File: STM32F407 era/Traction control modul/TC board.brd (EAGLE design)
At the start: 115.5 x 100 mm, 19 parts, among them IC1 74HC14D, IC2 lm2575, U1 MAX13052ESA+

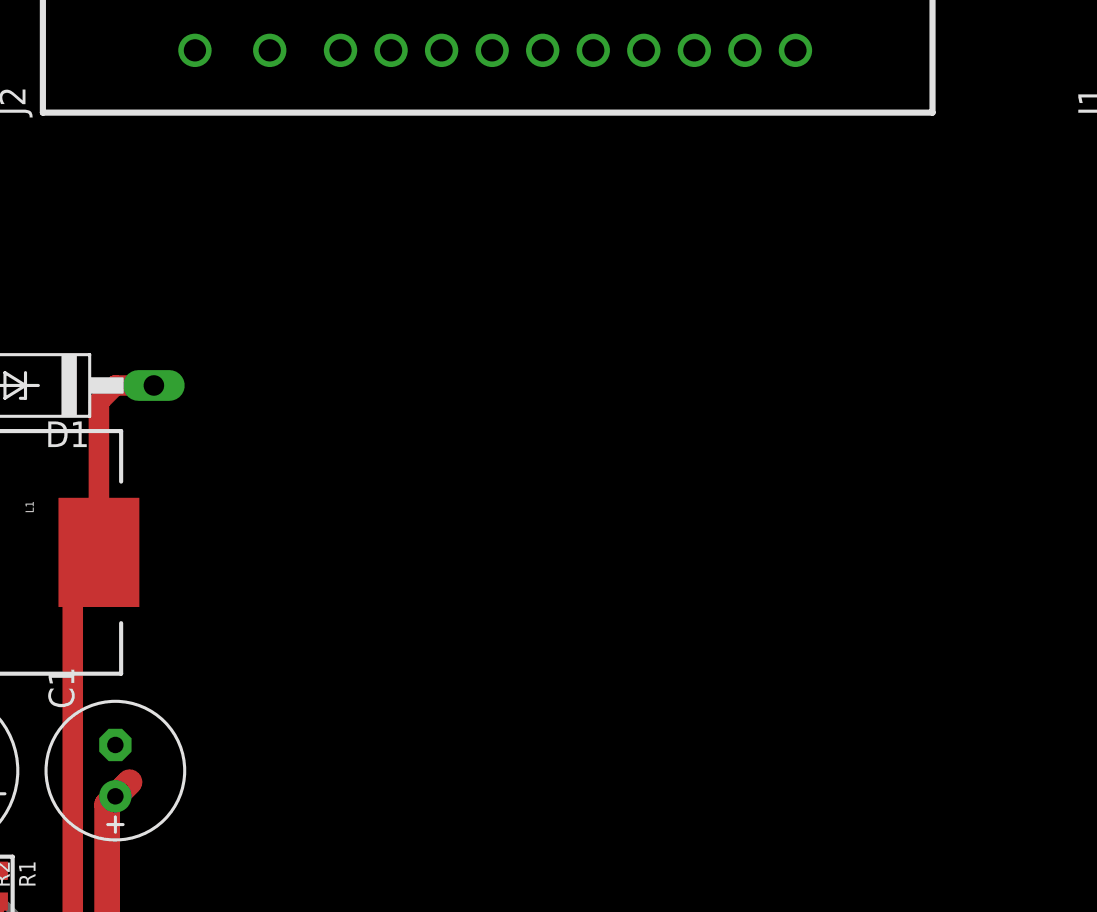
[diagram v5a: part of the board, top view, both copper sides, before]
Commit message: started working on control signals to gear
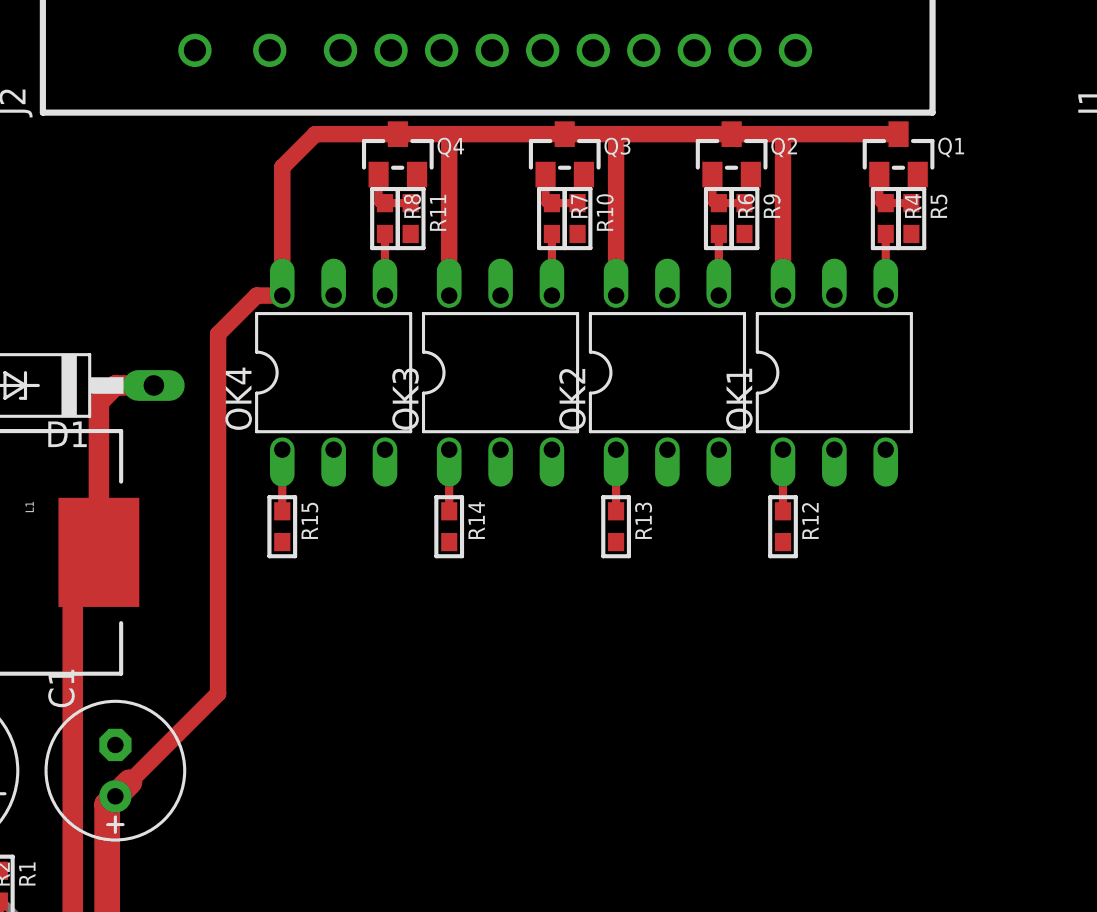
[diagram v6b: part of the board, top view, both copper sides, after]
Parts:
- added OK1, OK2, OK3, OK4: H11L1M, optocoupler:DIL06
- added Q1, Q2, Q3, Q4: (no value), microbuilder:SOT23-WIDE
- added R10, R11, R5, R9: 1000, microbuilder:_0603
- added R12, R13, R14, R15, R4, R6, R7, R8: 200, microbuilder:_0603
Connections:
- new net N$10: Q2.1, R6.1, R9.1
- new net N$11: OK3.4, R7.2
- new net N$12: Q3.1, R10.1, R7.1
- new net N$13: OK4.4, R8.2
- new net N$14: Q4.1, R11.1, R8.1
- new net N$15: OK4.1, R15.1
- new net N$16: OK3.1, R14.1
- new net N$17: OK2.1, R13.1
- new net N$18: OK1.1, R12.1
- new net N$19: R12.2
- new net N$20: R13.2
- new net N$21: R14.2
- new net N$22: R15.2
- new net N$7: OK1.4, R4.2
- new net N$8: Q1.1, R4.1, R5.1
- new net N$9: OK2.4, R6.2
- net 12V: now also OK1.6, OK2.6, OK3.6, OK4.6, Q1.3, Q2.3, Q3.3, Q4.3
- net GND: now also OK1.2, OK1.5, OK2.2, OK2.5, OK3.2, OK3.5, OK4.2, OK4.5, Q1.2, Q2.2, Q3.2, Q4.2, R10.2, R11.2, R5.2, R9.2
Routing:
- net 12V: track 11.6 -> 101.0 mm
- net N$9: track 0.00 -> 3.05 mm
- net N$7: track 0.00 -> 3.05 mm
- net N$18: track 0.00 -> 3.05 mm
- net N$17: track 0.00 -> 3.05 mm
- net N$16: track 0.00 -> 3.05 mm
- net N$15: track 0.00 -> 3.05 mm
- net N$13: track 0.00 -> 3.05 mm
- net N$11: track 0.00 -> 3.05 mm
- net N$8: track 0.00 -> 3.00 mm
- net N$10: track 0.00 -> 3.00 mm
- net N$12: track 0.00 -> 3.00 mm
- net N$14: track 0.00 -> 3.00 mm

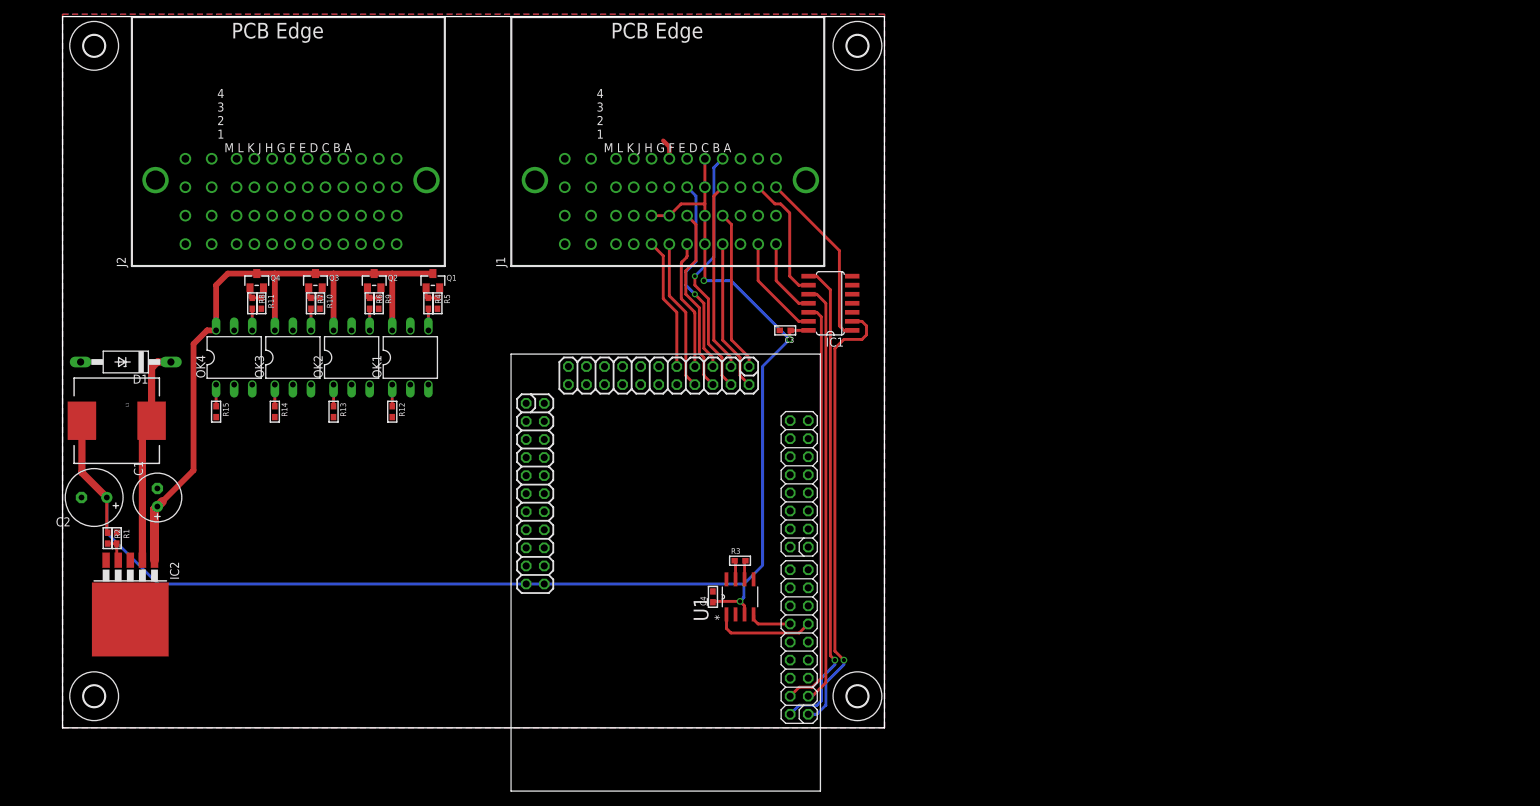
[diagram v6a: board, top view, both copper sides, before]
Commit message: succeded in removing one of 2 connectors
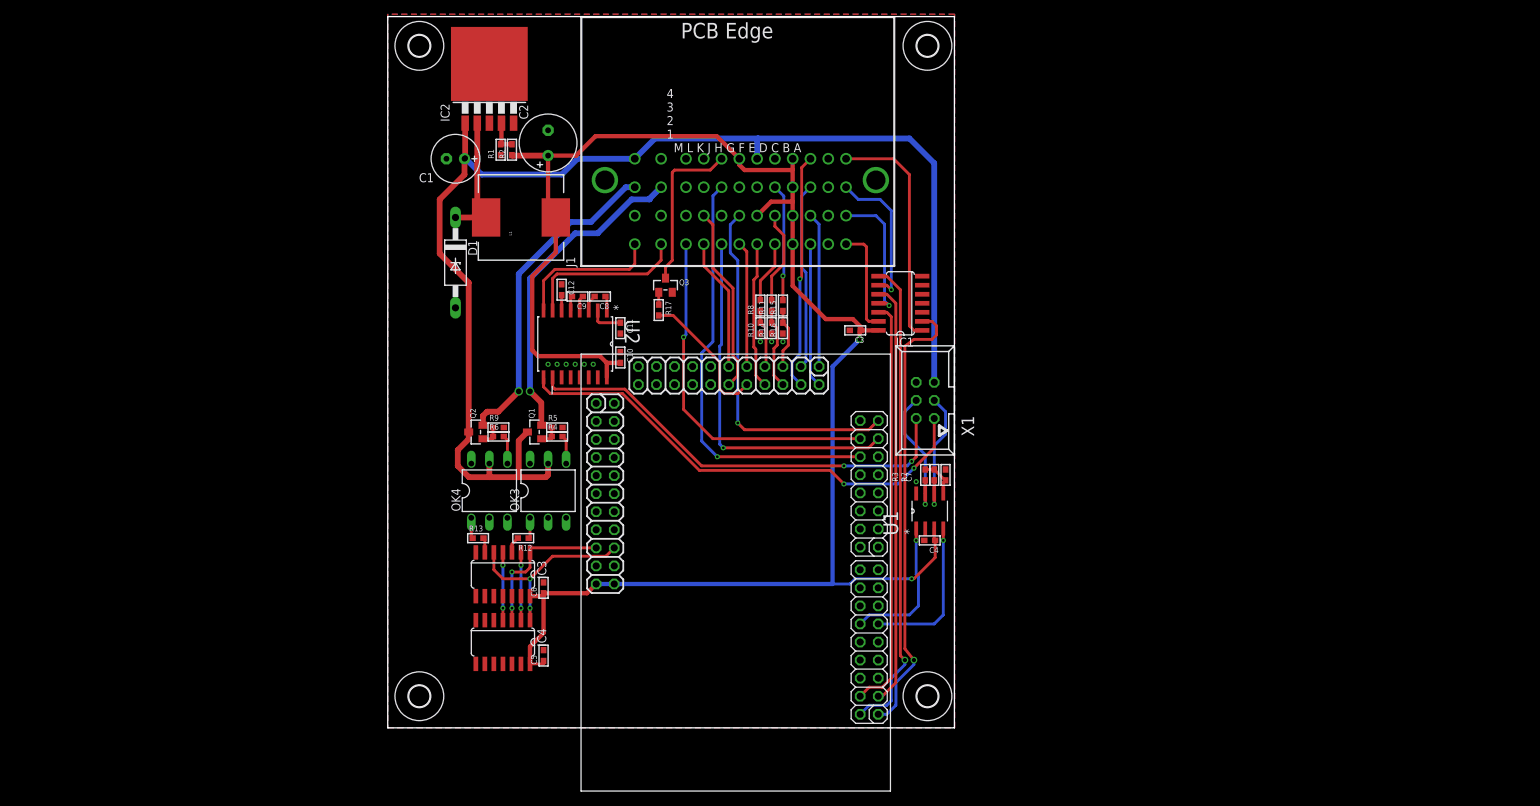
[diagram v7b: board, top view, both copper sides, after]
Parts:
- removed J2: (no value), unicorn_v2:AUTOCONNECTOR
- removed OK1, OK2: H11L1M, optocoupler:DIL06
- removed Q4: (no value), microbuilder:SOT23-WIDE
- added C10, C11, C12, C5, C6, C8, C9: 100n, microbuilder:_0603
- added C7: 4n7, microbuilder:_0603
- added IC3: 74AC08D, 74xx-eu:SO14
- added IC4: 74AC04D, 74xx-eu:SO14
- added R16: 178, microbuilder:_0603
- added R17: 500, microbuilder:_0603
- added U2: MAX232AEWE+, Maxim_By_element14_Batch_1:SOIC127P1032X265-16N
- added X1: 057-006-1, con-panduit:057-006-1
- J1: value (none) -> CON1
- OK3, OK4: value H11L1M -> 4N37
- R10: value 1000 -> 178
- R11: value 1000 -> 604
- R14: value 200 -> 178
- R15, R8: value 200 -> 604
- R3: value 1k8 -> 60
- R7: value 200 -> 60
- moved R7 90.9 mm to (76.8, 35.6), turned to 90 degrees
- moved IC2 88.8 mm to (14.3, 90.8), turned to 0 degrees
- moved R15 81.1 mm to (55.6, 59.4), turned to 90 degrees
- moved C2 81.0 mm to (22.5, 82.2), turned to 90 degrees
- moved R2 78.8 mm to (17.5, 81.3), turned to 90 degrees
- moved R1 76.8 mm to (15.9, 81.3), turned to 90 degrees
- moved R11 71.8 mm to (54.0, 59.4), turned to 90 degrees
- moved R8 71.4 mm to (52.4, 59.4), turned to 90 degrees
- moved R14 70.8 mm to (54.0, 56.2), turned to 90 degrees
- moved L1 63.6 mm to (18.7, 71.8), turned to 90 degrees
- moved C1 63.4 mm to (9.53, 80.0), turned to 180 degrees
- moved R10 62.0 mm to (52.4, 56.2), turned to 90 degrees
- moved Q3 49.2 mm to (39.1, 62.2)
- moved D1 48.4 mm to (9.53, 65.4), turned to 270 degrees
- moved H2 45.7 mm to (4.45, 95.9)
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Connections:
- new net BITEO: R15.1, R16.2, U$1.P$5
- new net BRAKEP: J1.K1, U$1.P$76
- new net COMRX: U2.9, X1.1
- new net COMTX: U2.10, X1.2
- new net DIRA: IC3.1, IC4.3, U$1.P$39
- new net DIRAO: J1.L3, Q1.2
- new net DIRB: IC3.5, IC4.1, U$1.P$40
- new net DIRBO: J1.M3, Q2.2
- new net FUEL1: J1.J3
- new net FUEL2: J1.K3
- new net FUEL3: J1.J4
- new net FUEL4: J1.K4
- new net GSENSO: R10.2, R8.1, U$1.P$7
- new net IGNCUT: R17.2, U$1.P$10
- new net IGNCUTO: J1.H4, Q3.3
- new net N$23: C11.1, U2.2
- new net N$24: Q3.1, R17.1
- new net NEUTRAL: J1.J1, U$1.P$11
- new net OILP: J1.J2, U$1.P$12
- new net RS232RX: J1.M1, U2.8
- new net RS232TX: J1.L1, U2.7
- new net SPEED: J1.G2, U$1.P$77
- new net VTEMP: J1.H1, U$1.P$75
- new net VTEMP2: J1.H3, U$1.P$74
- new net YAWO: R11.1, R14.2, U$1.P$6
- net 12V: now also J1.F4, J1.M4, OK3.5, OK4.5, X1.5; no longer J1.G4, J1.M1, OK1.6, OK2.6, OK3.6, OK4.6, Q3.3, Q4.3
- net 3.3V: now also C10.2, C5.1, C6.1, IC3.14, IC4.14, J1.D1, J1.D2, J1.D3, J1.D4, J1.F2, J1.G4, U2.16; no longer J1.E1, J1.E2, J1.E3, J1.E4, J1.G2, J1.H2
- net BITE: now also J1.E3, R15.2; no longer J1.F3, U$1.P$5
- net BRAKE-POT: now also J1.F1; no longer J1.G1
- net CANH: now also R7.1, X1.3; no longer R3.2
- net CANL: now also X1.4
- net CAN_RX: now also U1.4; no longer U1.1
- net CAN_TX: now also U1.1; no longer U1.4
- net CLUTCH-POT: now also J1.G1; no longer J1.H1
- net GND: now also C10.1, C11.2, C12.1, C5.2, C6.2, C7.2, IC3.10, IC3.12, IC3.13, IC3.7, IC3.9, IC4.11, IC4.13, IC4.5, IC4.7, IC4.9, J1.B1, J1.B3, J1.E4, J1.F3, J1.H2, J1.L4, R10.1, R14.1, R16.1, U2.15, X1.6; no longer J1.A2, J1.A4, J1.C1, J1.C2, J1.C3, J1.C4, J1.F4, J1.H3, J1.L1, OK1.2, OK1.5, OK2.2, OK2.5, OK3.5, OK4.5, Q1.2, Q2.2, Q4.2, R10.2, R11.2
- net GSENS: now also J1.E1, R8.2; no longer J1.F1, U$1.P$7
- net N$11: now also IC3.6, R13.2; no longer OK3.4, R7.2
- net N$12: now also C7.1, R3.2, R7.2, U1.5; no longer Q3.1, R10.1, R7.1
- net N$13: now also C12.2, U2.6; no longer OK4.4, R8.2
- net N$14: now also C9.1, U2.4; no longer Q4.1, R11.1, R8.1
- net N$15: now also IC3.4, IC4.4; no longer OK4.1, R15.1
- net N$16: now also IC3.2, IC4.2; no longer OK3.1, R14.1
- net N$17: now also OK4.1; no longer OK2.1
- net N$18: now also OK3.1; no longer OK1.1
- net N$19: now also IC3.3
- net N$20: now also C9.2, U2.5; no longer R13.2
- net N$21: now also C8.2, U2.3; no longer R14.2
- net N$22: now also C8.1, U2.1; no longer R15.2
- net N$3: now also IC1.9, J1.A3; no longer IC1.11, J1.A1
- net N$4: now also J1.A1; no longer J1.B1
- net N$5: now also J1.A4; no longer J1.A3
- net N$6: now also IC1.11, J1.A2; no longer IC1.9, J1.B3
- net N$7: now also OK3.4; no longer OK1.4
- net N$9: now also OK4.4; no longer OK2.4
- net TRAVEL1: now also J1.C2; no longer J1.D2
- net TRAVEL2: now also J1.C1; no longer J1.D1
- net TRAVEL3: now also J1.C3; no longer J1.D3
- net TRAVEL4: now also J1.C4; no longer J1.D4
- net YAW: now also J1.E2, R11.2; no longer J1.F2, U$1.P$6
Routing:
- net 12V: track 101.0 -> 180.0 mm, vias 0 -> 1
- net COMRX: track 0.00 -> 68.1 mm, vias 0 -> 2
- net COMTX: track 0.00 -> 63.0 mm, vias 0 -> 2
- net VTEMP2: track 0.00 -> 60.1 mm, vias 0 -> 1
- net VTEMP: track 0.00 -> 51.3 mm, vias 0 -> 1
- net SPEED: track 0.00 -> 50.8 mm, vias 0 -> 1
- net BRAKEP: track 0.00 -> 49.9 mm, vias 0 -> 1
- net DIRBO: track 0.00 -> 45.7 mm, vias 0 -> 1
- net DIRAO: track 0.00 -> 45.1 mm, vias 0 -> 1
- net 3.3V: track 205.2 -> 239.6 mm, vias 3 -> 2
- net DIRB: track 0.00 -> 28.1 mm, vias 0 -> 2
- net OILP: track 0.00 -> 26.2 mm
- net RS232TX: track 0.00 -> 23.1 mm
- net IGNCUTO: track 0.00 -> 23.0 mm
- net DIRA: track 0.00 -> 21.6 mm, vias 0 -> 2
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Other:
- board size 115.5 x 100 mm -> 79.7 x 100 mm

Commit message: moved outfaced boards to new folder
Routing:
- net N$3: track 20.9 -> 16.7 mm, vias 1 -> 0
- net N$6: track 19.2 -> 15.8 mm, vias 1 -> 0
- net N$4: track 15.0 -> 13.9 mm
- net 12V: track 180.0 -> 180.3 mm, vias 1 -> 0
